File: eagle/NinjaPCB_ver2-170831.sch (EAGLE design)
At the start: 65 parts, among them IC1 MCP3551SNNC, IC2 VNH5019/VNH3SP30NC, J2 WELL_TEMP, J3 HEATER, J4 HEATER_TEMP, J5 HEATER_TEMP, Q2 IRF520NPBF, Q3 IRF520NPBF, U1 CJT1117-3.3-SOT223

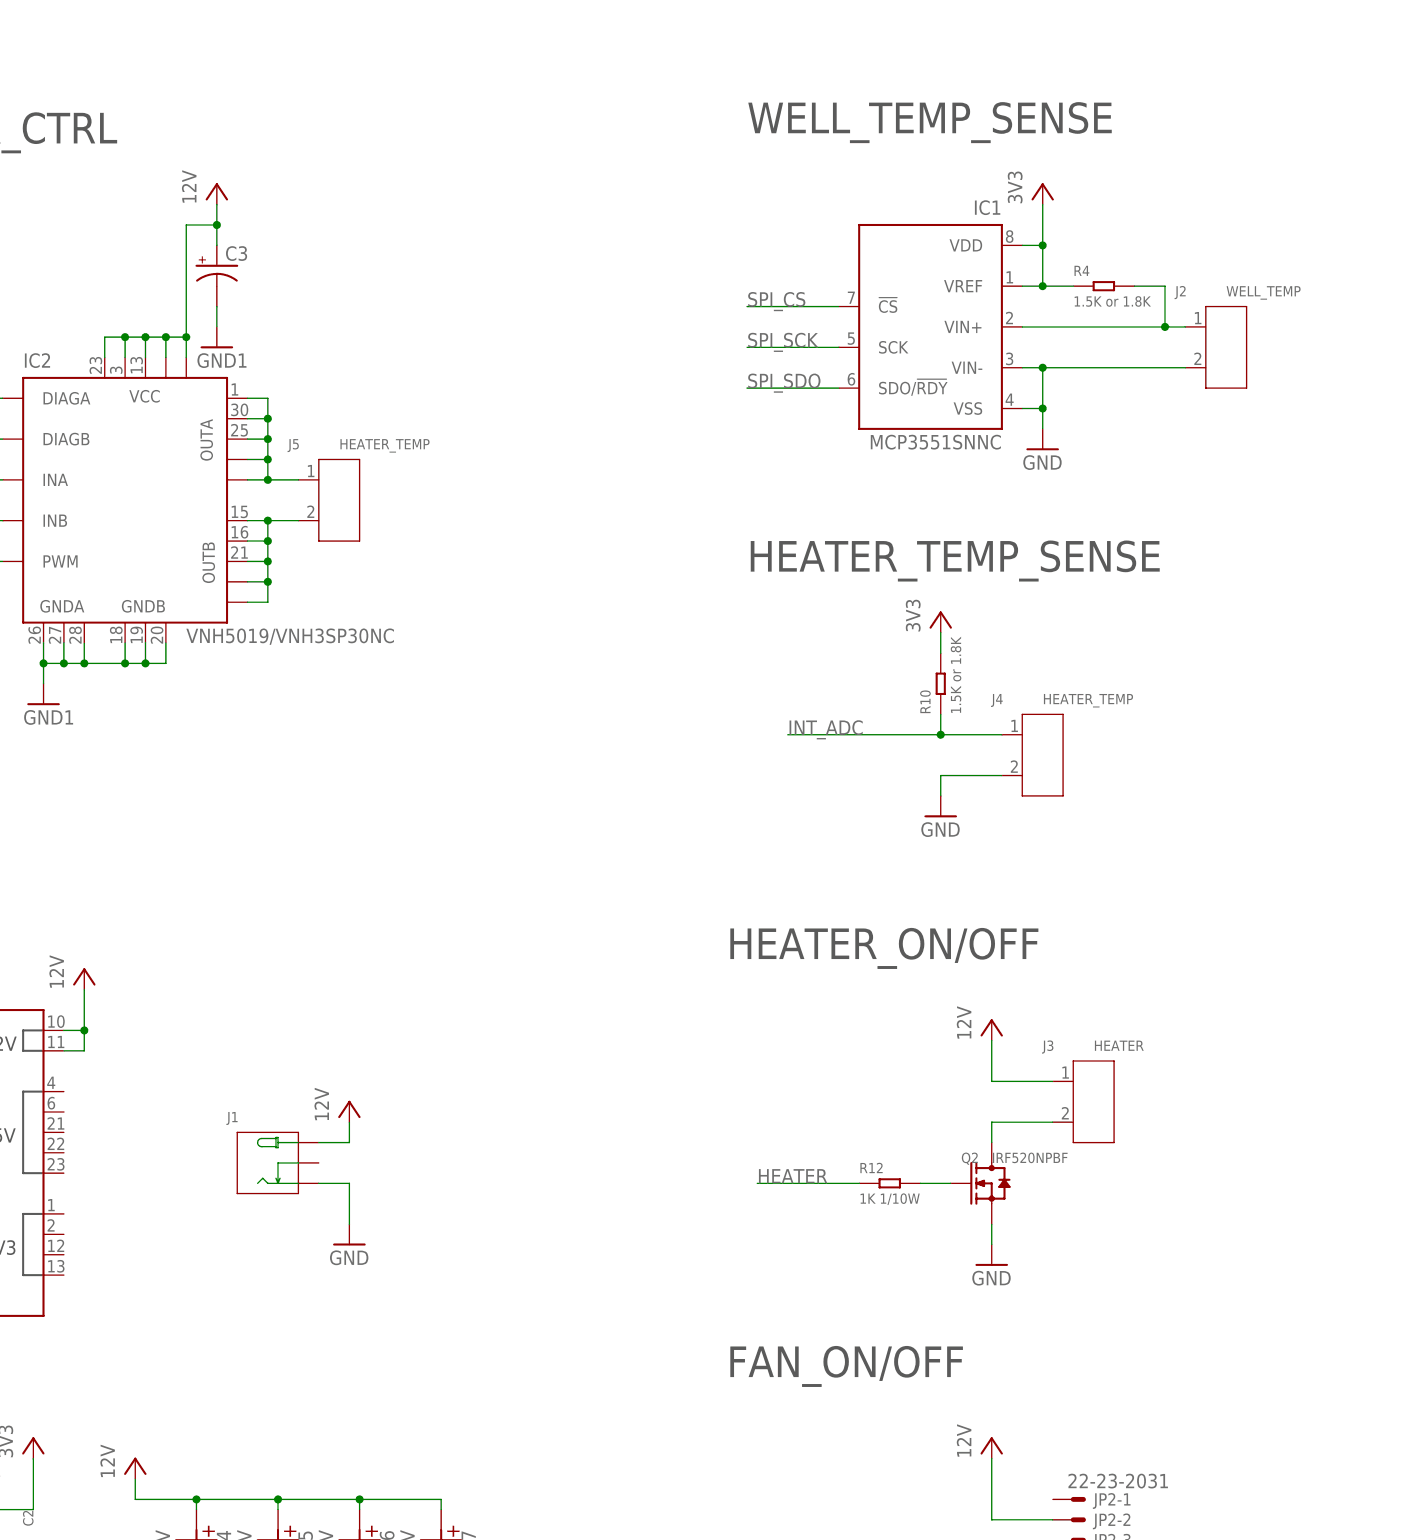
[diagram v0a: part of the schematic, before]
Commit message: preparing NinjaPCB ver2 using Seeed OPL
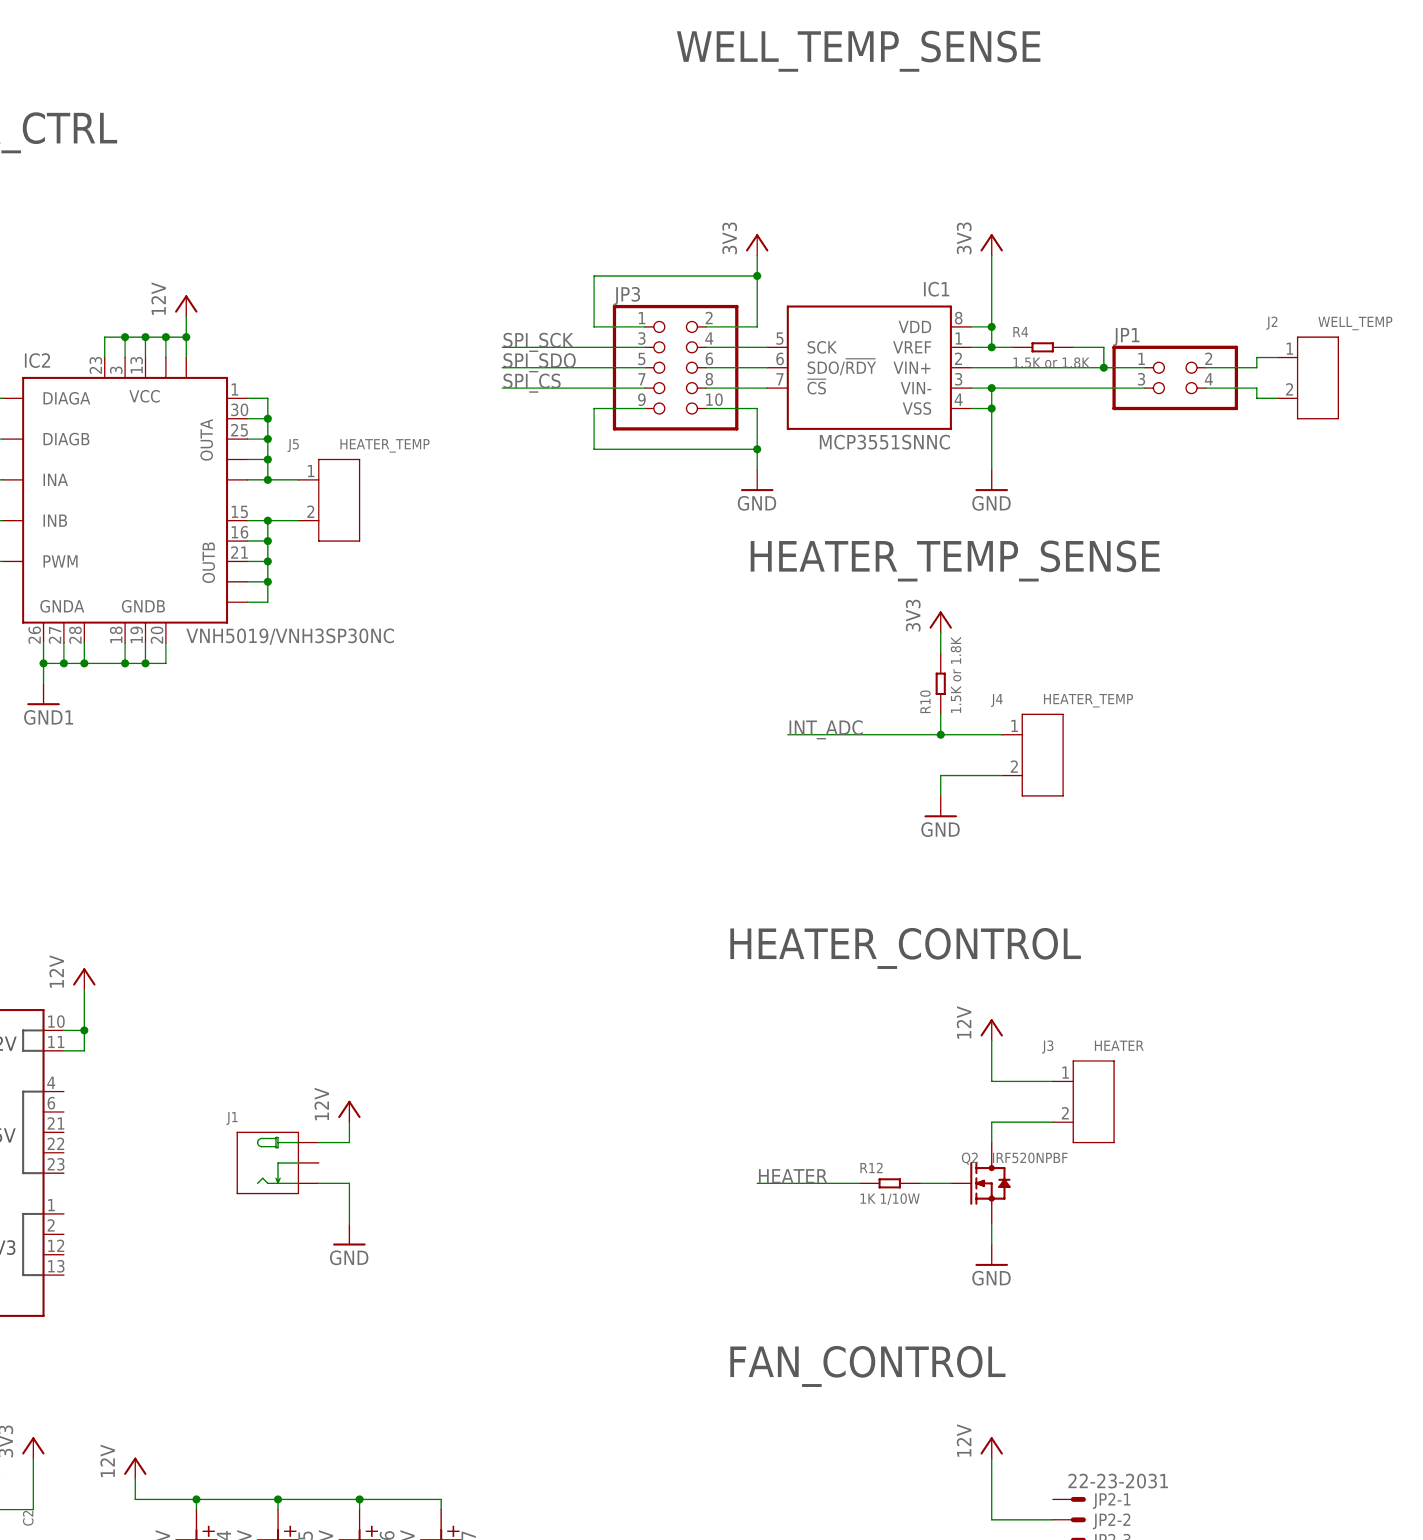
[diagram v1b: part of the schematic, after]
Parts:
- removed C3: (no value), rcl:CPOL-USE5-13
- added JP1: (no value), pinhead:PINHD-2X2
- added JP3: (no value), pinhead:PINHD-2X5
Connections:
- removed net VCC: SJ16.1
- new net N$85: J2.2, JP1.4
- new net N$86: J2.1, JP1.2
- new net N$90: IC1.SCK, JP3.4
- new net N$91: IC1.SDO/!RDY, JP3.6
- new net N$92: IC1.!CS, JP3.8
- net 12V: no longer C3.+
- net 3V3: now also JP3.1, JP3.2, SJ16.1
- net GND: now also JP1.3, JP3.10, JP3.9; no longer J2.2
- net GND1: no longer C3.-
- net N$1: now also JP1.1; no longer J2.1
- net SPI_CS: now also JP3.7; no longer IC1.!CS
- net SPI_SCK: now also JP3.3; no longer IC1.SCK
- net SPI_SDO: now also JP3.5; no longer IC1.SDO/!RDY
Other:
- note added: "FAN_CONTROL"
- note added: "HEATER_CONTROL"
- note removed: "FAN_ON/OFF"
- note removed: "HEATER_ON/OFF"
- moved on the sheet: IC1, J2, R4

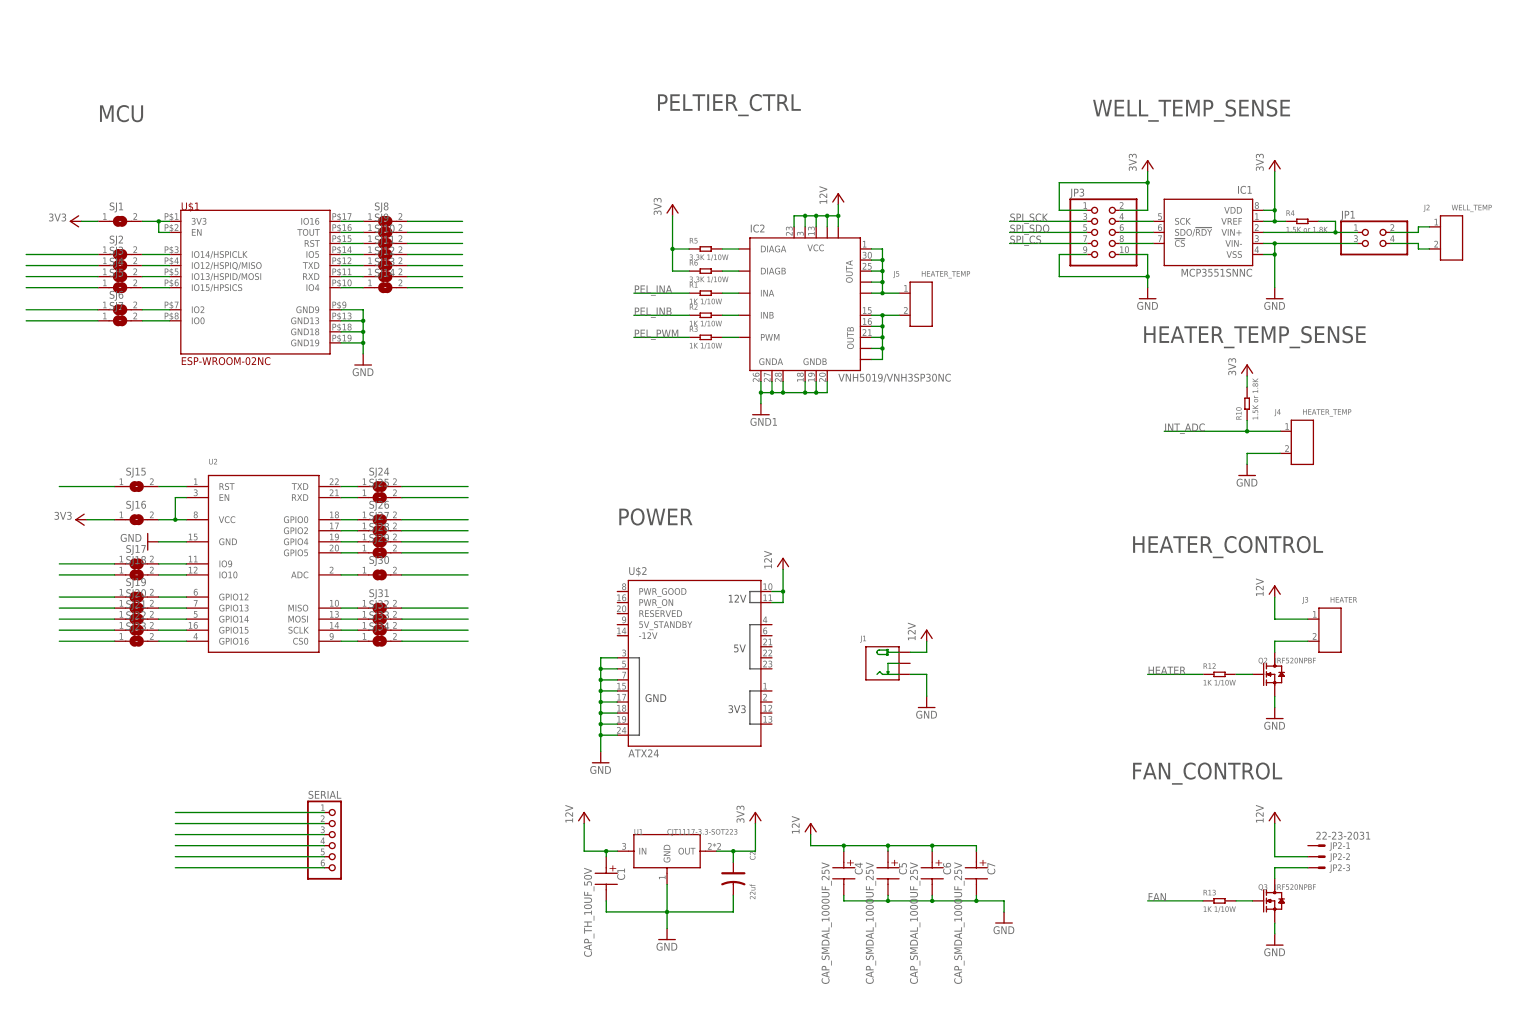
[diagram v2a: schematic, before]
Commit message: add evaluation board for NinjaPCB ver2
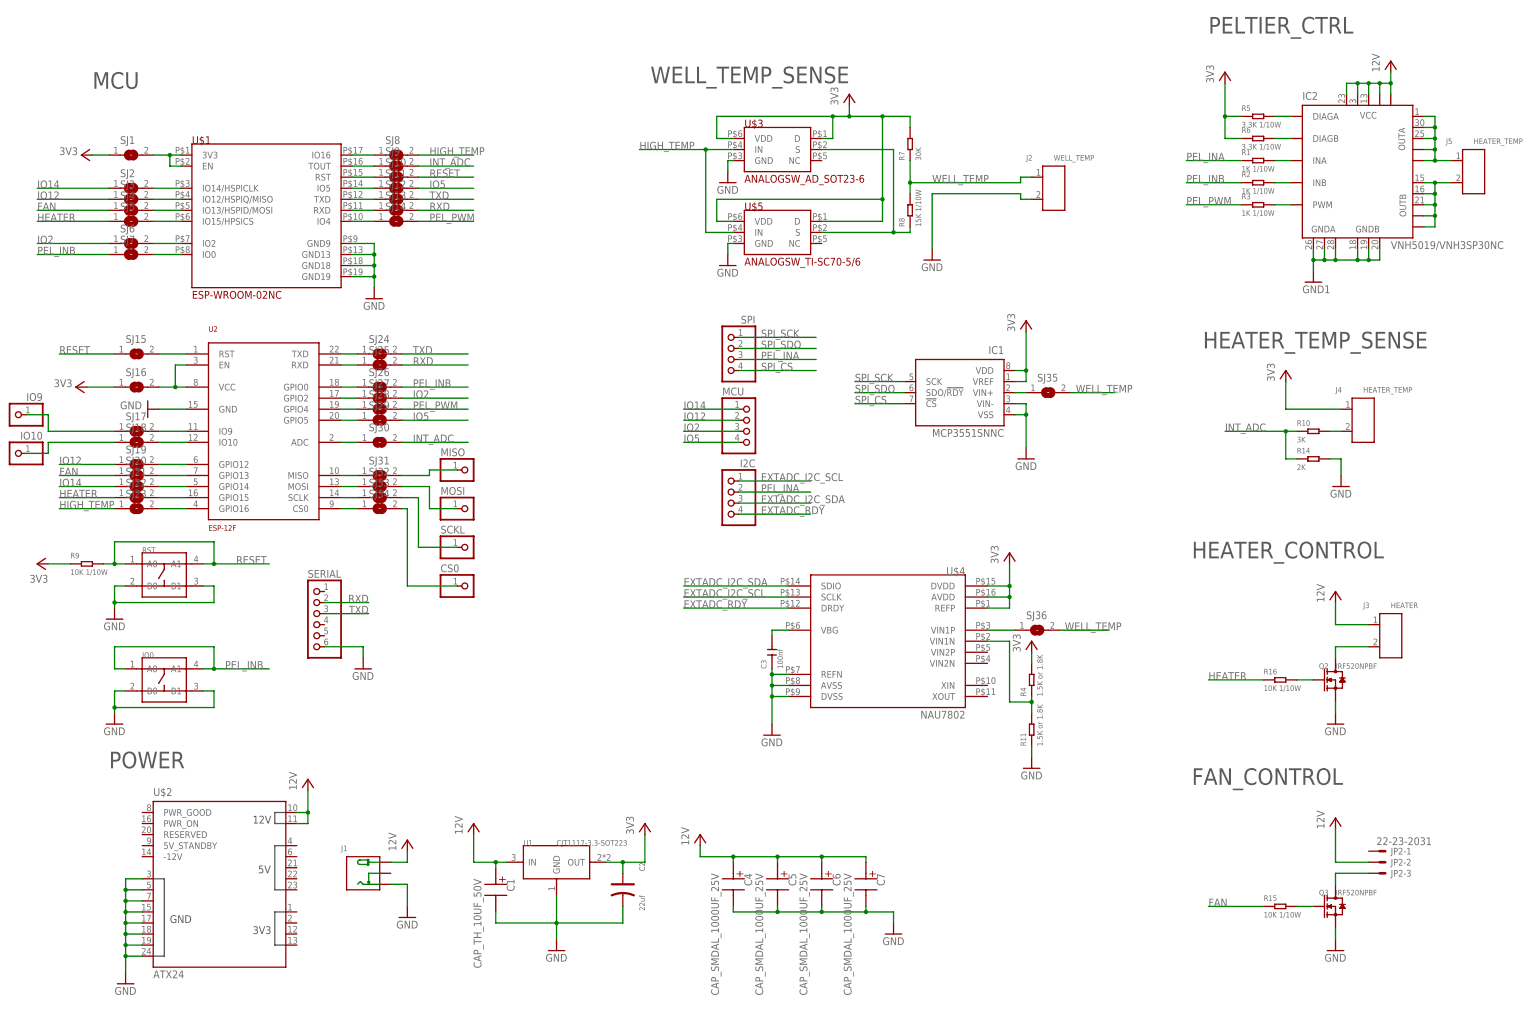
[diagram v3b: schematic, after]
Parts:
- removed JP1: (no value), pinhead:PINHD-2X2
- removed JP3: (no value), pinhead:PINHD-2X5
- removed R12, R13: 1K 1/10W, Seeed-Resistor:SMD-RES-1K-5%-1/10W(0603)
- added C3: 100nf, Seeed-Capacitor:CERAMIC-100NF-50V-10%-X7R(0603)
- added CS0, IO10, IO9, MISO, MOSI, SCKL: (no value), pinhead:PINHD-1X1
- added I2C, MCU, SPI: (no value), pinhead:PINHD-1X4OCT
- added IO0, RST: (no value), Seeed-Switch:DIP-SWITCH-TACTILE-SPST-NO/TS-1109(4P-D6.0MM)'TS-1109'
- added R11: 1.5K or 1.8K, Seeed-Resistor:SMD-RES-1.5K-1%-1/10W(0603)
- added R14: 2K, Seeed-Resistor:SMD-RES-2K-1%-1/10W(0603)
- added R15, R16, R9: 10K 1/10W, Seeed-Resistor:SMD-RES-10K-5%-1/10W(0603)
- added R7: 30K, Seeed-Resistor:SMD-RES-30K-1%-1/10W(0603)
- added R8: 15K 1/10W, Seeed-Resistor:SMD-RES-15K-1%-1/10W(0603)
- added SJ35, SJ36: (no value), jumper:SJ
- added U$3: ANALOGSW_AD_SOT23-6, PCR-IC:ANALOGSW_AD_SOT23-6
- added U$4: NAU7802, PCR-IC:NAU7802
- added U$5: ANALOGSW_TI-SC70-5/6, PCR-IC:ANALOGSW_TI-SC70-5/6
- R10: value 1.5K or 1.8K -> 3K; device Seeed-Resistor:SMD-RES-1.5K-1%-1/10W(0603) -> Seeed-Resistor:SMD-RES-3K-1%-1/10W(0603)
- U2: value (none) -> ESP-12F
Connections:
- removed net N$26: SJ8.2
- removed net N$28: SJ10.2
- removed net N$30: SJ12.2
- removed net N$33: SJ14.2
- removed net N$34: SJ7.1
- removed net N$35: SJ6.1
- removed net N$36: SJ5.1
- removed net N$37: SJ4.1
- removed net N$38: SJ3.1
- removed net N$39: SJ2.1
- removed net N$41: SJ15.1
- removed net N$54: SJ24.2
- removed net N$55: SJ25.2
- removed net N$56: SJ26.2
- removed net N$57: SJ27.2
- removed net N$58: SJ28.2
- removed net N$59: SJ29.2
- removed net N$60: SJ30.2
- removed net N$74: SJ19.1
- removed net N$75: SJ20.1
- removed net N$76: SJ21.1
- removed net N$77: SJ22.1
- removed net N$78: SJ23.1
- removed net N$79: SERIAL.6
- removed net N$80: SERIAL.5
- removed net N$81: SERIAL.4
- removed net N$82: SERIAL.3
- removed net N$83: SERIAL.2
- removed net N$84: SERIAL.1
- removed net N$85: J2.2, JP1.4
- removed net N$86: J2.1, JP1.2
- removed net N$90: IC1.SCK, JP3.4
- new net EXTADC_I2C_SCL: I2C.1, U$4.SCLK
- new net EXTADC_I2C_SDA: I2C.3, U$4.SDIO
- new net EXTADC_RDY: I2C.4, U$4.DRDY
- new net HIGH_TEMP: SJ23.1, SJ8.2, U$3.IN, U$5.IN
- new net IO12: MCU.2, SJ19.1, SJ3.1
- new net IO14: MCU.1, SJ2.1, SJ21.1
- new net IO2: MCU.3, SJ27.2, SJ6.1
- new net IO5: MCU.4, SJ11.2, SJ29.2
- new net RESET: R9.2, RST.A0, RST.A1, SJ10.2, SJ15.1
- new net RXD: SERIAL.2, SJ13.2, SJ25.2
- new net TXD: SERIAL.3, SJ12.2, SJ24.2
- new net VCC: R9.1
- new net WELL_TEMP: J2.1, R7.1, R8.2, SJ35.2, SJ36.2
- net 3V3: now also J4.1, R4.2, R7.2, U$3.D, U$3.VDD, U$4.AVDD, U$4.DVDD, U$4.REFP, U$5.D, U$5.VDD; no longer JP3.1, JP3.2, R10.2, R4.1
- net FAN: now also R15.1, SJ20.1, SJ4.1; no longer R13.1
- net GND: now also C3.1, IO0.B0, IO0.B1, J2.2, R11.1, R14.2, RST.B0, RST.B1, SERIAL.6, U$3.GND, U$4.AVSS, U$4.DVSS, U$4.REFN, U$5.GND; no longer J4.2, JP1.3, JP3.10, JP3.9
- net HEATER: now also R16.1, SJ22.1, SJ5.1; no longer R12.1
- net INT_ADC: now also R14.1, SJ30.2, SJ9.2; no longer J4.1
- net N$1: now also J4.2, R10.2; no longer IC1.VIN+, JP1.1, R4.2
- net N$27: now also R8.1, U$3.S, U$5.S; no longer SJ9.2
- net N$29: now also SJ36.1, U$4.VIN1P; no longer SJ11.2
- net N$3: now also R16.2; no longer R12.2
- net N$31: now also IC1.VIN+, SJ35.1; no longer SJ13.2
- net N$5: now also R15.2; no longer R13.2
- net N$61: now also MISO.1
- net N$62: now also MOSI.1
- net N$63: now also SCKL.1
- net N$64: now also CS0.1
- net N$72: now also IO9.1
- net N$73: now also IO10.1
- net N$91: now also R11.2, R4.1, U$4.VIN1N; no longer IC1.SDO/!RDY, JP3.6
- net N$92: now also C3.2, U$4.VBG; no longer IC1.!CS, JP3.8
- net PEL_INA: now also I2C.2, SPI.3
- net PEL_INB: now also IO0.A0, IO0.A1, SJ26.2, SJ7.1
- net PEL_PWM: now also SJ14.2, SJ28.2
- net SPI_CS: now also IC1.!CS, SPI.4; no longer JP3.7
- net SPI_SCK: now also IC1.SCK, SPI.1; no longer JP3.3
- net SPI_SDO: now also IC1.SDO/!RDY, SPI.2; no longer JP3.5
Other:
- moved on the sheet: C1, C2, C4, C5, C6, C7, IC1, IC2, J1, J2, J3, J4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
